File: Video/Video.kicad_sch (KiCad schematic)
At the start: 1 part

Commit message: Video card added...
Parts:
- added SYNC_GENERATOR: ATF2500C-20PC, symbol PC:ATF2500C-40P6
- added U?: ATF22V10C, Package_DIP:DIP-24_W7.62mm_Socket_LongPads, symbol PC:ATF22V10C
- added X?: ACO-10MHz, Oscillator:Oscillator_DIP-14, symbol Oscillator:ACO-xxxMHz
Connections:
- net +5V: now also SYNC_GENERATOR.10 (VCC)
- net A10: now also U?.7 (IN)
- net A11: now also U?.6 (IN)
- net A12: now also U?.5 (IN)
- net A13: now also U?.4 (IN/PD)
- net A14: now also U?.3 (IN)
- net A15: now also U?.2 (IN)
- net A4: now also U?.14 (I/O)
- net A5: now also U?.13 (IN)
- net A6: now also U?.11 (IN)
- net A7: now also U?.10 (IN)
- net A8: now also U?.9 (IN)
- net A9: now also U?.8 (IN)
- net GND: now also SYNC_GENERATOR.30 (GND), U?.12 (GND)
- net PHI2: now also U?.1 (CLK/IN)
- net R/~{W}: now also U?.23 (I/O)
- net +12v: no longer names the net of J?.36 (Pin_36)
- net -12v: no longer names the net of J?.38 (Pin_38)
- new net: SYNC_GENERATOR.1 (CLK/IN), X?.8 (OUT)
- new net VCC: U?.24 (VCC)
- new net ~{RAM_OE}: U?.22 (I/O)
- new net ~{RAM_WE}: U?.21 (I/O)
- no-connect marks 1 -> 3

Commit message: Added components...
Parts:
- added U?: IDT7134, symbol PC:IDT7134
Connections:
- net +5V: now also U?.24 (VCC), X?.14 (Vcc), U?.2 (R/WL)
- net A0: now also U?.42 (A0R)
- net A1: now also U?.41 (A1R)
- net A10: now also U?.44 (A10R); no longer U?.7 (IN)
- net A11: now also U?.45 (A11R); no longer U?.6 (IN)
- net A2: now also U?.40 (A2R)
- net A3: now also U?.39 (A3R)
- net A4: now also U?.38 (A4R); no longer U?.14 (I/O)
- net A5: now also U?.37 (A5R); no longer U?.13 (IN)
- net A6: now also U?.36 (A6R); no longer U?.11 (IN)
- net A7: now also U?.35 (A7R); no longer U?.10 (IN)
- net A8: now also U?.34 (A8R); no longer U?.9 (IN)
- net A9: now also U?.33 (A9R); no longer U?.8 (IN)
- net D0: now also U?.32 (I/O7R)
- net D1: now also U?.31 (I/O6R)
- net D2: now also U?.30 (I/O5R)
- net D3: now also U?.29 (I/O4R)
- net D4: now also U?.28 (I/O3R)
- net D5: now also U?.27 (I/O2R)
- net D6: now also U?.26 (I/O1R)
- net D7: now also U?.25 (I/O0R)
- net GND: now also X?.7 (GND), U?.24 (GND)
- net PHI2: now also U?.47 (/CER)
- net R/~{W}: now also U?.6 (IN), U?.46 (R/WR); no longer U?.23 (I/O)
- net VCC: now also U?.48 (VCC); no longer U?.24 (VCC)
- net DA2: now reaches SYNC_GENERATOR.17 (IN)
- net DA2: now also U?.18 (I/O2L)
- net DA3: now reaches SYNC_GENERATOR.18 (IN)
- net DA3: now also U?.19 (I/O3L)
- net DA4: now reaches SYNC_GENERATOR.19 (IN)
- net DA4: now also U?.20 (I/O4L)
- net DA0: now reaches SYNC_GENERATOR.2 (IN)
- net DA0: now also U?.16 (I/O0L)
- net DA5: now reaches SYNC_GENERATOR.20 (IN)
- net DA5: now also U?.21 (I/O5L)
- net DA6: now reaches SYNC_GENERATOR.21 (IN)
- net DA6: now also U?.22 (I/O6L)
- net DA7: now reaches SYNC_GENERATOR.22 (IN)
- net DA7: now also U?.23 (I/O7L)
- net DA1: now reaches SYNC_GENERATOR.3 (IN)
- net DA1: now also U?.17 (I/O1L)
- net 8MHz: no longer names the net of J?.26 (Pin_26)
- net CLK: no longer names the net of J?.20 (Pin_20)
- net PHI1: no longer names the net of J?.22 (Pin_22)
- net RDY: no longer names the net of J?.30 (Pin_30)
- net SYNC: no longer names the net of J?.32 (Pin_32)
- net ~{IRQ}: no longer names the net of J?.34 (Pin_34)
- net ~{RAM_OE}: no longer names the net of U?.22 (I/O)
- net ~{RAM_WE}: no longer names the net of U?.21 (I/O)
- new net RD: U?.23 (I/O), U?.43 (/OER)
- no-connect marks 3 -> 9
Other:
- moved on the sheet: SYNC_GENERATOR, U?, X?

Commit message: Added reference files...
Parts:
- added J?: DB15_Female_HighDensity, symbol Connector:DB15_Female_HighDensity
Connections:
- net PHI2: no longer U?.47 (/CER)
- net RD: now also U?.22 (I/O); no longer U?.23 (I/O)
- net R/~{W}: now also U?.23 (I/O); no longer U?.46 (R/WR), U?.6 (IN)
- net at SYNC_GENERATOR.29 (I/O23): now also U?.1 (/CEL), U?.5 (/OEL)
- net LA11: now reaches SYNC_GENERATOR.31 (I/O11)
- net LA11: now also U?.3 (A11L)
- net LA10: now reaches SYNC_GENERATOR.32 (I/O10)
- net LA10: now also U?.4 (A10L)
- net LA9: now reaches SYNC_GENERATOR.33 (I/O9)
- net LA9: now also U?.15 (A9L)
- net LA8: now reaches SYNC_GENERATOR.34 (I/O8)
- net LA8: now also U?.14 (A8L)
- net LA7: now reaches SYNC_GENERATOR.35 (I/O7)
- net LA7: now also U?.13 (A7L)
- net LA6: now reaches SYNC_GENERATOR.36 (I/O6)
- net LA6: now also U?.12 (A6L)
- net LA0: now reaches SYNC_GENERATOR.4 (I/O0)
- net LA0: now also U?.6 (A0L)
- net LA1: now reaches SYNC_GENERATOR.5 (I/O1)
- net LA1: now also U?.7 (A1L)
- net LA2: now reaches SYNC_GENERATOR.6 (I/O2)
- net LA2: now also U?.8 (A2L)
- net LA3: now reaches SYNC_GENERATOR.7 (I/O3)
- net LA3: now also U?.9 (A3L)
- net LA4: now reaches SYNC_GENERATOR.8 (I/O4)
- net LA4: now also U?.10 (A4L)
- net LA5: now reaches SYNC_GENERATOR.9 (I/O5)
- net LA5: now also U?.11 (A5L)
- net ~{VGA_EN}: now reaches U?.20 (I/O)
- net ~{VGA_EN}: now also U?.47 (/CER)
- net WR: now reaches U?.21 (I/O)
- net WR: now also U?.46 (R/WR)
- net DA0 renamed LD0
- net DA1 renamed LD1
- net DA2 renamed LD2
- net DA3 renamed LD3
- net DA4 renamed LD4
- net DA5 renamed LD5
- net DA6 renamed LD6
- net DA7 renamed LD7

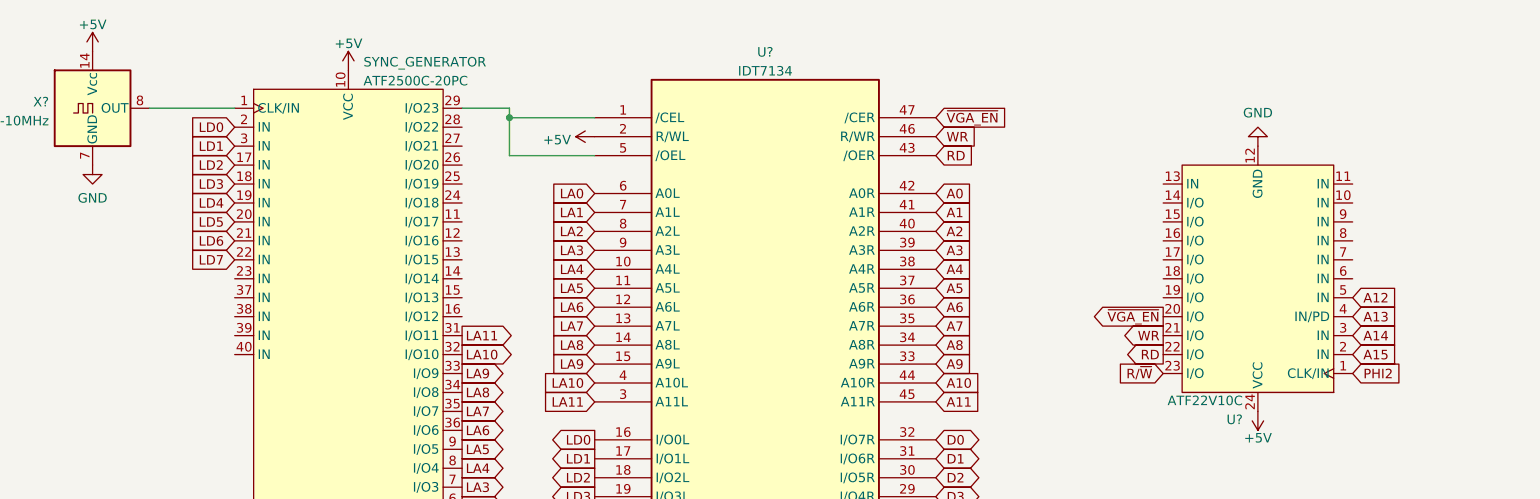
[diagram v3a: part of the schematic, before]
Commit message: Updated motherboard and video card schematics...
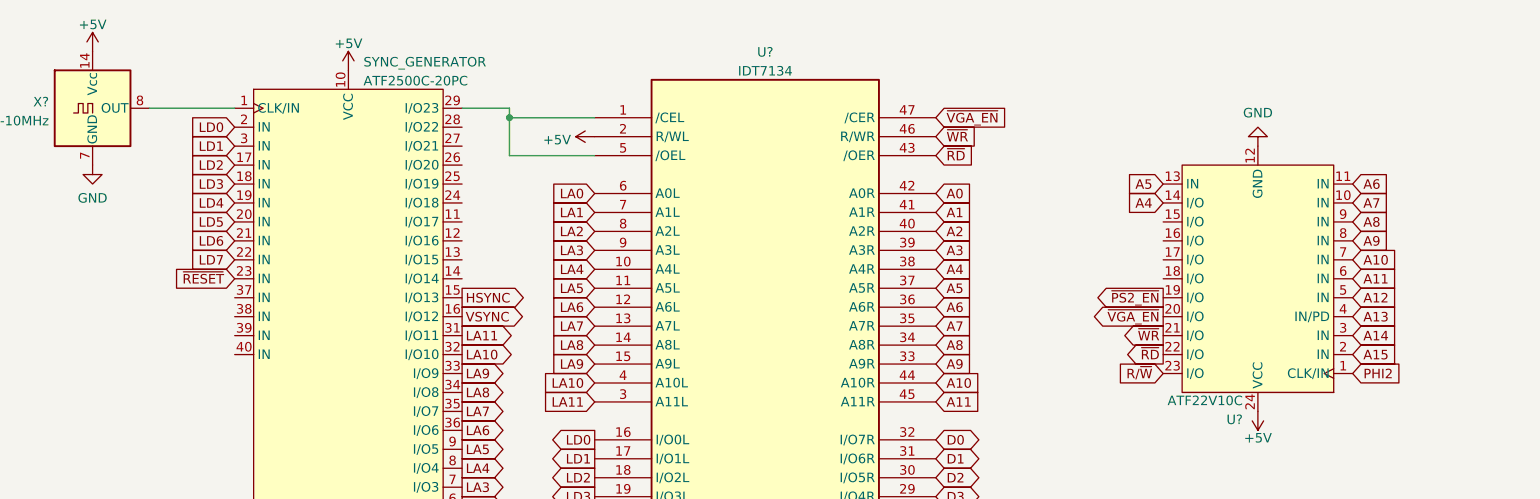
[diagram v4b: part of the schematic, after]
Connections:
- net A10: now also U?.7 (IN)
- net A11: now also U?.6 (IN)
- net A4: now also U?.14 (I/O)
- net A5: now also U?.13 (IN)
- net A6: now also U?.11 (IN)
- net A7: now also U?.10 (IN)
- net A8: now also U?.9 (IN)
- net A9: now also U?.8 (IN)
- net ~{RESET}: now also SYNC_GENERATOR.23 (IN)
- net HSYNC: now reaches SYNC_GENERATOR.15 (I/O13)
- net VSYNC: now reaches SYNC_GENERATOR.16 (I/O12)
- net ~{PS2_EN}: now reaches U?.19 (I/O)
- net RD renamed ~{RD}
- net WR renamed ~{WR}
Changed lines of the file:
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@@
+    )
+  )
+  (global_label "~{PS2_EN}" (shape output) (at 181.61 66.04 180) (fields_autoplaced)
+    (effects (font (size 1.27 1.27)) (justify right))
+    (property "Intersheet References" "${INTERSHEET_REFS}" (id 0) (at 172.0607 65.9606 0)
+      (effects (font (size 1.27 1.27)) (justify right) hide)
     )
   )
@@
     )
   )
+  (global_label "A11" (shape input) (at 207.01 63.5 0) (fields_autoplaced)
+    (effects (font (size 1.27 1.27)) (justify left))
+    (property "Intersheet References" "${INTERSHEET_REFS}" (id 0) (at 212.9307 63.4206 0)
+      (effects (font (size 1.27 1.27)) (justify left) hide)
+    )
+  )
   (global_label "LA2" (shape input) (at 105.41 57.15 180) (fields_autoplaced)
     (effects (font (size 1.27 1.27)) (justify right))
@@
     )
   )
+  (global_label "A9" (shape input) (at 207.01 58.42 0) (fields_autoplaced)
+    (effects (font (size 1.27 1.27)) (justify left))
+    (property "Intersheet References" "${INTERSHEET_REFS}" (id 0) (at 211.7212 58.3406 0)
+      (effects (font (size 1.27 1.27)) (justify left) hide)
+    )
+  )
   (global_label "LA11" (shape input) (at 105.41 80.01 180) (fields_autoplaced)
     (effects (font (size 1.27 1.27)) (justify right))
@@
     )
   )
-  (global_label "WR" (shape input) (at 151.13 44.45 0) (fields_autoplaced)
+  (global_label "~{WR}" (shape input) (at 151.13 44.45 0) (fields_autoplaced)
     (effects (font (size 1.27 1.27)) (justify left))
     (property "Intersheet References" "${INTERSHEET_REFS}" (id 0) (at 156.2645 44.3706 0)
@@
     )
   )
-  (global_label "RD" (shape input) (at 151.13 46.99 0) (fields_autoplaced)
+  (global_label "A8" (shape input) (at 207.01 55.88 0) (fields_autoplaced)
+    (effects (font (size 1.27 1.27)) (justify left))
+    (property "Intersheet References" "${INTERSHEET_REFS}" (id 0) (at 211.7212 55.8006 0)
+      (effects (font (size 1.27 1.27)) (justify left) hide)
+    )
+  )
+  (global_label "~{RD}" (shape input) (at 151.13 46.99 0) (fields_autoplaced)
     (effects (font (size 1.27 1.27)) (justify left))
     (property "Intersheet References" "${INTERSHEET_REFS}" (id 0) (at 156.0831 46.9106 0)
@@
     )
   )
+  (global_label "HSYNC" (shape output) (at 87.63 66.04 0) (fields_autoplaced)
+    (effects (font (size 1.27 1.27)) (justify left))
+    (property "Intersheet References" "${INTERSHEET_REFS}" (id 0) (at 96.2721 65.9606 0)
+      (effects (font (size 1.27 1.27)) (justify left) hide)
+    )
+  )
   (global_label "A8" (shape input) (at 151.13 72.39 0) (fields_autoplaced)
     (effects (font (size 1.27 1.27)) (justify left))
@@
     )
   )
+  (global_label "VSYNC" (shape output) (at 87.63 68.58 0) (fields_autoplaced)
+    (effects (font (size 1.27 1.27)) (justify left))
+    (property "Intersheet References" "${INTERSHEET_REFS}" (id 0) (at 96.0302 68.5006 0)
+      (effects (font (size 1.27 1.27)) (justify left) hide)
+    )
+  )
   (global_label "LD0" (shape input) (at 57.15 43.18 180) (fields_autoplaced)
     (effects (font (size 1.27 1.27)) (justify right))
@@
     )
   )
-  (global_label "WR" (shape output) (at 181.61 71.12 180) (fields_autoplaced)
+  (global_label "~{WR}" (shape output) (at 181.61 71.12 180) (fields_autoplaced)
     (effects (font (size 1.27 1.27)) (justify right))
     (property "Intersheet References" "${INTERSHEET_REFS}" (id 0) (at 176.4755 71.0406 0)
@@
     )
   )
-  (global_label "RD" (shape output) (at 181.61 73.66 180) (fields_autoplaced)
+  (global_label "~{RD}" (shape output) (at 181.61 73.66 180) (fields_autoplaced)
     (effects (font (size 1.27 1.27)) (justify right))
     (property "Intersheet References" "${INTERSHEET_REFS}" (id 0) (at 176.6569 73.5806 0)
@@
     )
   )
+  (global_label "A6" (shape input) (at 207.01 50.8 0) (fields_autoplaced)
+    (effects (font (size 1.27 1.27)) (justify left))
+    (property "Intersheet References" "${INTERSHEET_REFS}" (id 0) (at 211.7212 50.7206 0)
+      (effects (font (size 1.27 1.27)) (justify left) hide)
+    )
+  )
   (global_label "A9" (shape output) (at 241.3 68.58 180) (fields_autoplaced)
     (effects (font (size 1.27 1.27)) (justify right))
@@
     )
   )
+  (global_label "~{RESET}" (shape input) (at 57.15 63.5 180) (fields_autoplaced)
+    (effects (font (size 1.27 1.27)) (justify right))
+    (property "Intersheet References" "${INTERSHEET_REFS}" (id 0) (at 48.9917 63.4206 0)
+      (effects (font (size 1.27 1.27)) (justify right) hide)
+    )
+  )
+  (global_label "A10" (shape input) (at 207.01 60.96 0) (fields_autoplaced)
+    (effects (font (size 1.27 1.27)) (justify left))
+    (property "Intersheet References" "${INTERSHEET_REFS}" (id 0) (at 212.9307 60.8806 0)
+      (effects (font (size 1.27 1.27)) (justify left) hide)
+    )
+  )
+  (global_label "A7" (shape input) (at 207.01 53.34 0) (fields_autoplaced)
+    (effects (font (size 1.27 1.27)) (justify left))
+    (property "Intersheet References" "${INTERSHEET_REFS}" (id 0) (at 211.7212 53.2606 0)
+      (effects (font (size 1.27 1.27)) (justify left) hide)
+    )
+  )
   (global_label "LA0" (shape output) (at 87.63 99.06 0) (fields_autoplaced)
     (effects (font (size 1.27 1.27)) (justify left))
@@
     )
   )
+  (global_label "A5" (shape input) (at 181.61 50.8 180) (fields_autoplaced)
+    (effects (font (size 1.27 1.27)) (justify right))
+    (property "Intersheet References" "${INTERSHEET_REFS}" (id 0) (at 176.8988 50.7206 0)
+      (effects (font (size 1.27 1.27)) (justify right) hide)
+    )
+  )
   (global_label "LA11" (shape output) (at 87.63 71.12 0) (fields_autoplaced)
     (effects (font (size 1.27 1.27)) (justify left))
@@
     )
   )
+  (global_label "A4" (shape input) (at 181.61 53.34 180) (fields_autoplaced)
+    (effects (font (size 1.27 1.27)) (justify right))
+    (property "Intersheet References" "${INTERSHEET_REFS}" (id 0) (at 176.8988 53.2606 0)
+      (effects (font (size 1.27 1.27)) (justify right) hide)
+    )
+  )
